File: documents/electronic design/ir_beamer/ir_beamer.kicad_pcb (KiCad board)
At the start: 2 copper layers, 42 parts, among them P1 Via, P10 Via, P2 Via, P3 Via, P4 Via, P5 Via, P7 Via, P8 Via, P9 Via, T1 2N7002K, T10 2N7002K, T11 2N7002K, T12 2N7002K, T2 2N7002K, T3 2N7002K, T4 2N7002K, T5 2N7002K, T6 2N7002K, T7 2N7002K, T8 2N7002K, T9 2N7002K, U1 74HC595D, U2 STM32F103HEADER, U3 74HC595D, U4 SE8R01_module

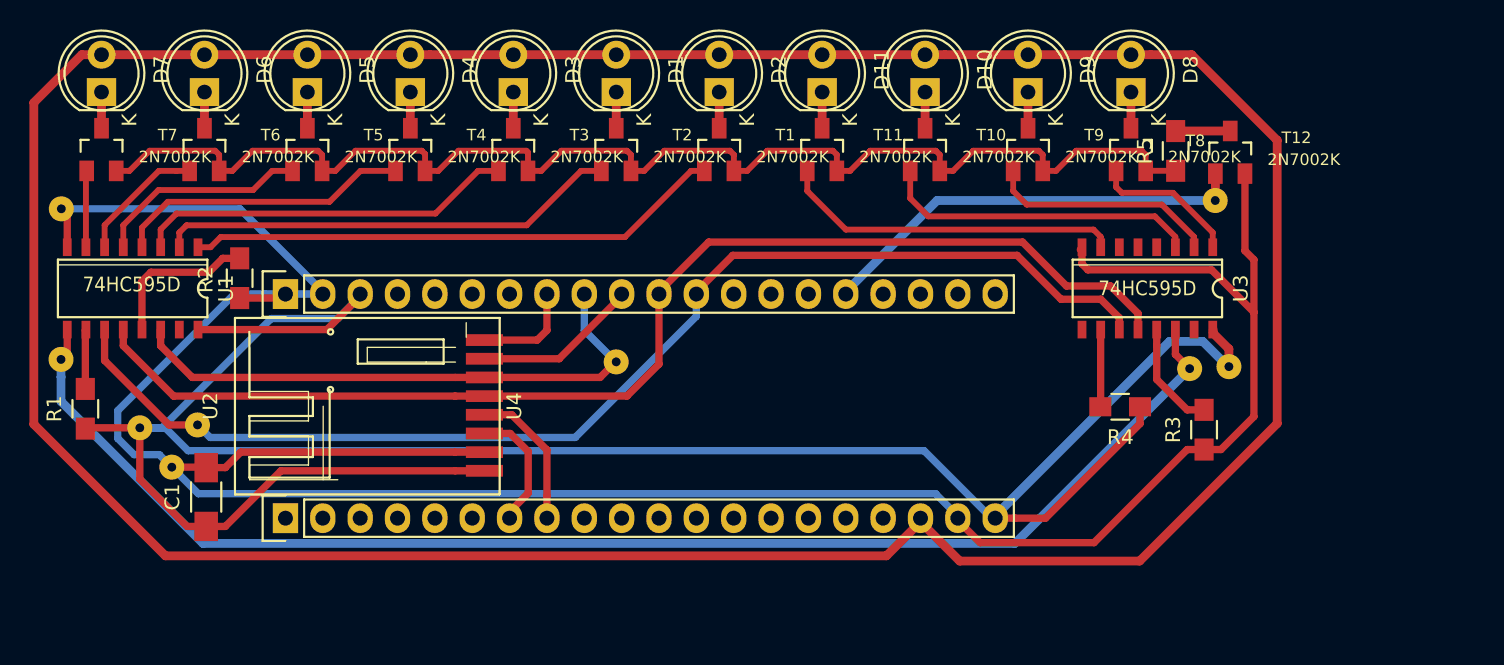
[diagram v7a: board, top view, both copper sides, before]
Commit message: update PCB projects for beamer and sensor
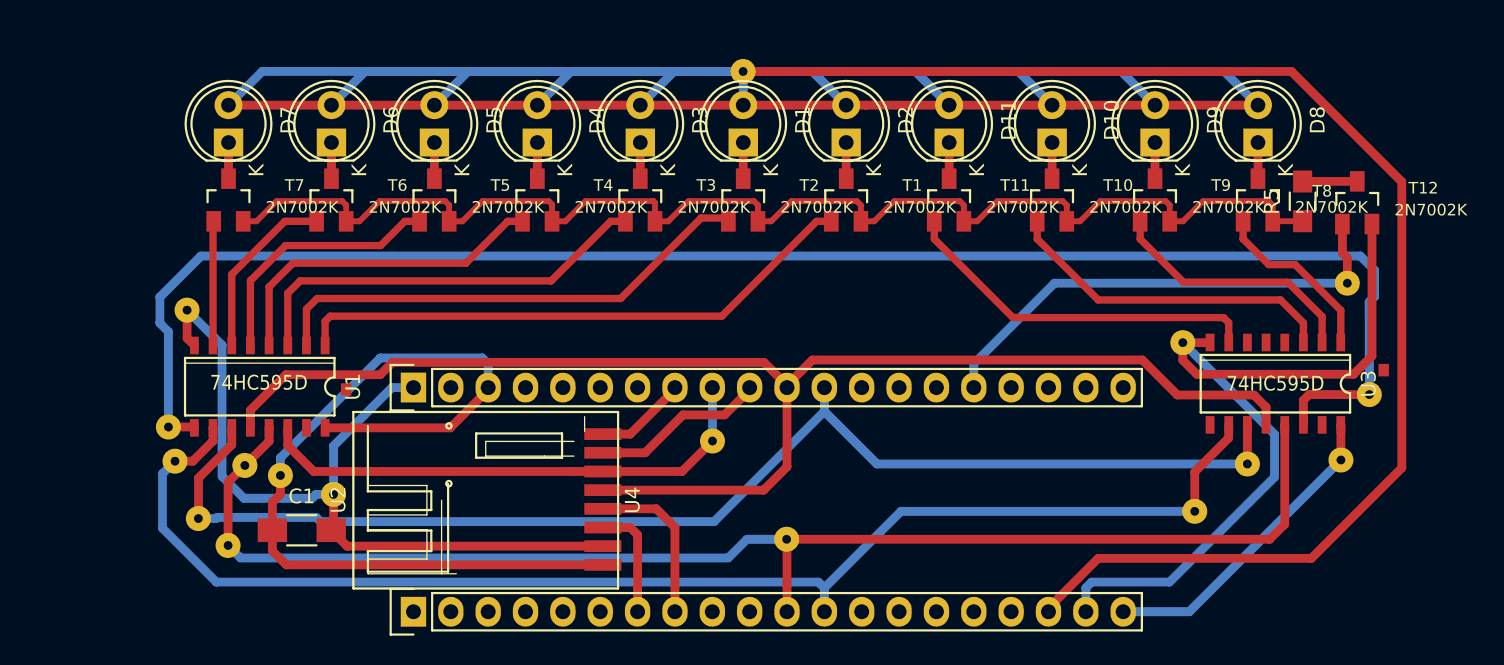
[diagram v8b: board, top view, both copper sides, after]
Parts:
- removed R1, R2, R3, R4: 4.7k, Resistors_SMD:R_0805_HandSoldering
- added P11: Via, footprints:Via, F.Cu at (25.5, 47.6)
- added P12: Via, footprints:Via, F.Cu at (67.1, 52.9)
- added P13: Via, footprints:Via, F.Cu at (94.9, 51.0)
- added P14: Via, footprints:Via, F.Cu at (98.5, 47.8)
- added P15: Via, footprints:Via, F.Cu at (29.1, 53.3)
- added P16: Via, footprints:Via, F.Cu at (94.1, 39.5)
- added P17: Via, footprints:Via, F.Cu at (64.2, 21.1)
- added P6: Via, footprints:Via, F.Cu at (30.3, 47.9)
- moved P7 12.3 mm to (106.7, 43.0)
- moved P4 11.2 mm to (36.3, 49.8)
- moved P10 11.0 mm to (26.4, 37.3)
- moved U1 10.9 mm to (31.3, 42.5)
- moved U3 10.9 mm to (100.4, 42.3)
- moved U2 10.8 mm to (41.7, 57.8)
- moved P3 10.6 mm to (105.2, 35.5)
- moved U4 10.3 mm to (55.7, 56.2)
- moved P5 10.1 mm to (32.7, 48.5)
- moved P9 9.92 mm to (104.8, 47.5)
- moved D7 9.29 mm to (29.2, 25.9)
- moved T7 9.29 mm to (29.2, 29.8)
- moved D6 9.29 mm to (36.2, 25.9)
- moved T6 9.29 mm to (36.2, 29.8)
- moved D1 9.29 mm to (64.2, 25.9)
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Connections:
- net Net-(P7-Pad1) renamed Cascade
- U1 pad 10: Net-(R1-Pad2) -> MR_NOT
- U1 pad 13: Net-(R2-Pad2) -> OE_NOT
- U2 pad 11: (no net) -> OE_NOT
- U2 pad 12: (no net) -> MR_NOT
- U3 pad 10: Net-(R4-Pad2) -> MR_NOT
- U3 pad 13: Net-(R3-Pad2) -> OE_NOT
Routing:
- net +5V: track 223.9 -> 382.9 mm
- net OE_NOT: track 0.00 -> 94.2 mm
- net MR_NOT: track 0.00 -> 91.6 mm
- net +3V3: track 164.8 -> 82.1 mm
- net GND: track 182.6 -> 110.2 mm
- net Cascade: track 94.2 -> 109.9 mm
- net SPI_SCK: track 81.9 -> 94.2 mm
- net Net-(R2-Pad2): track 10.6 -> 0.00 mm
- net Net-(R3-Pad2): track 7.46 -> 0.00 mm
- net Latch: track 82.1 -> 87.9 mm
- net Net-(R4-Pad2): track 5.33 -> 0.00 mm
- net Net-(R1-Pad2): track 4.11 -> 0.00 mm
- net IR_PWM: track 29.7 -> 33.4 mm
- net SPI_MOSI: track 38.9 -> 35.3 mm
- net IR_LED_7: track 5.23 -> 8.55 mm
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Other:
- net class Default: trace_width 0.4 -> 0.6
- board text added: "."
